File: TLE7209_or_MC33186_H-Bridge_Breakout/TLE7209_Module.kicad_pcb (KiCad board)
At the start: 2 copper layers, 43 x 22 mm, 13 parts, among them J1 Conn_02x06_Odd_Even, J3 Conn_01x01, U1 TLE7209-2R

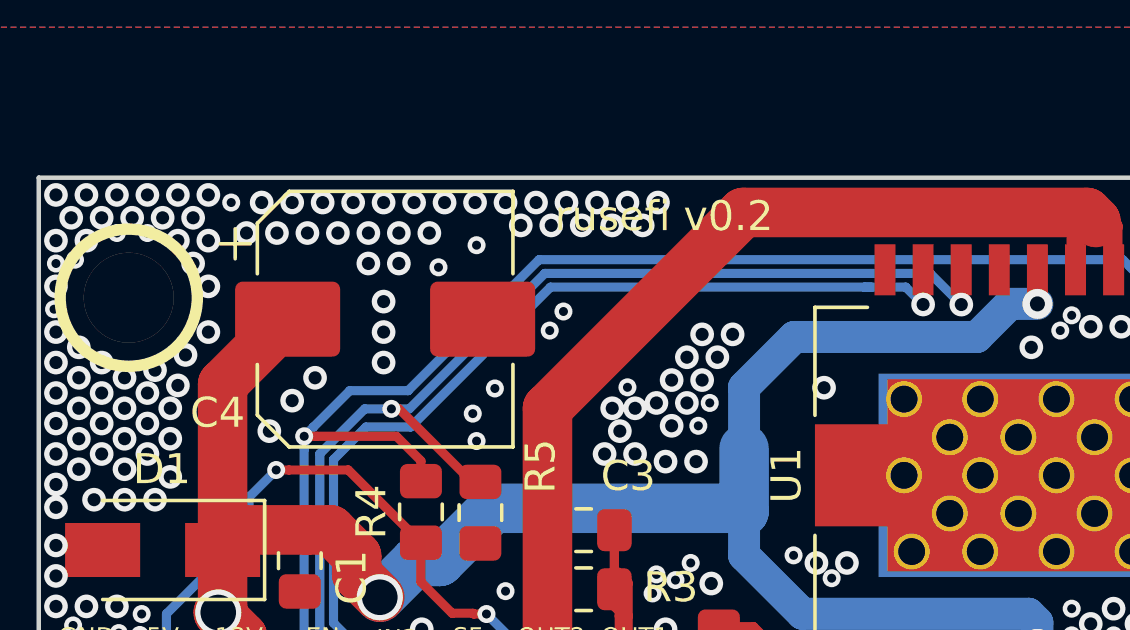
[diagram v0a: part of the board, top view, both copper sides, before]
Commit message: C4 value notes 100uf on schematic and PCB silk R4 & R5 now note 2.2K generated schematic PDF as 0.3
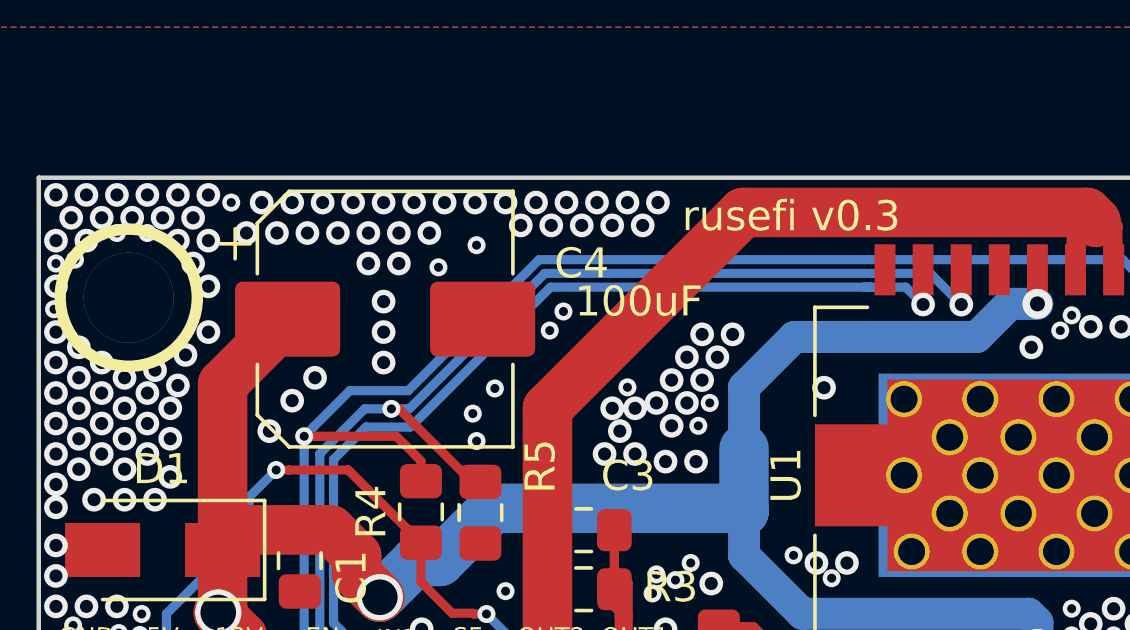
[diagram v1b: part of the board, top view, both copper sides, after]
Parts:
- C4: value CP1 -> 100uF
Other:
- board text added: "rusefi v0.3"
- board text removed: "rusefi v0.2"
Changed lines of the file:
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@@
-(kicad_pcb (version 20171130) (host pcbnew "(5.1.0-rc2-21-g16b3c80a7)")
+(kicad_pcb (version 20171130) (host pcbnew "(5.1.5)-3")
   (general
     (thickness 1.6)
@@
   (title_block
     (title "TLE7209-2R Module")
-    (date 2019-01-31)
-    (rev R0.2)
+    (date 2020-04-05)
+    (rev R0.3)
+    (company rusEFI)
   )
   (layers
@@
     (46 B.CrtYd user)
     (47 F.CrtYd user)
-    (48 B.Fab user hide)
-    (49 F.Fab user hide)
+    (48 B.Fab user)
+    (49 F.Fab user)
   )
   (setup
-    (last_trace_width 0.3048)
+    (last_trace_width 0.1524)
     (user_trace_width 0.1524)
     (user_trace_width 0.2159)
@@
     (tags "capacitor electrolytic")
     (attr smd)
-    (fp_text reference C4 (at -5.588 3.1242) (layer F.SilkS)
-      (effects (font (size 1 1) (thickness 0.15)))
-    )
-    (fp_text value CP1 (at 0 5.2) (layer F.Fab)
+    (fp_text reference C4 (at 6.5532 -1.8542) (layer F.SilkS)
+      (effects (font (size 1 1) (thickness 0.15)))
+    )
+    (fp_text value 100uF (at 8.4582 -0.5842 180) (layer F.SilkS)
       (effects (font (size 1 1) (thickness 0.15)))
     )
@@
   )
   (gr_circle (center 46.4312 36.9062) (end 46.9392 37.4142) (layer F.SilkS) (width 0.25))
-  (gr_text "rusefi v0.2" (at 40.8432 21.2852) (layer F.SilkS)
+  (gr_text "rusefi v0.3" (at 45.085 21.2852) (layer F.SilkS)
     (effects (font (size 1 1) (thickness 0.15)))
   )
